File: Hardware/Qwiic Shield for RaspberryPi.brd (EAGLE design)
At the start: 52.3 x 23 mm, 22 parts, among them J1 Qwiic Right Angle, J6 Qwiic Right Angle, J7 Qwiic Right Angle, J8 Qwiic Right Angle, U2 3.3V/600mA, U3 RASPBERRY_PI

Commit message: post design review
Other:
- board text added: "v10"
- board text removed: "v01"
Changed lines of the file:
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@@
 <wire x1="51.816" y1="11.811" x2="51.308" y2="12.319" width="0.3048" layer="22"/>
 <wire x1="51.308" y1="11.303" x2="51.816" y2="11.811" width="0.3048" layer="22"/>
-<text x="48.641" y="0.508" size="1.27" layer="16" font="vector" ratio="15" rot="MR0">v01</text>
+<text x="48.641" y="0.508" size="1.27" layer="16" font="vector" ratio="15" rot="MR0">v10</text>
 <text x="21.59" y="-26.67" size="1.778" layer="51" font="vector">A. England</text>
 <dimension x1="0" y1="0" x2="0" y2="22.86" x3="-8.89" y3="11.43" textsize="1.778" layer="47" unit="inch"/>

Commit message: Updated PROD_ID of 2x20
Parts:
- U3: value RASPBERRY_PI -> (none)
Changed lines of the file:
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@@
 <element name="U$1" library="SparkFun-Aesthetics" package="SFE_LOGO_FLAME_.1" value="SFE_LOGO_FLAME.1_INCH" x="5.334" y="4.445" rot="MR0"/>
 <element name="U$2" library="SparkFun-Aesthetics" package="SFE_LOGO_NAME_.1" value="SFE_LOGO_NAME.1_INCH" x="40.767" y="4.318"/>
-<element name="U3" library="SparkFun-Connectors" package="RASPBERRY_PI_SHIELD_BOTTOM_ENTRY_NOHOLES" value="RASPBERRY_PI" x="-6.35" y="13.97"/>
+<element name="U3" library="SparkFun-Connectors" package="RASPBERRY_PI_SHIELD_BOTTOM_ENTRY_NOHOLES" value="" x="-6.35" y="13.97">
+<attribute name="PROD_ID" value="CONN-13790" x="-6.35" y="13.97" size="1.778" layer="27" display="off"/>
+<attribute name="VALUE" value="" x="-6.35" y="13.97" size="1.778" layer="27" display="off"/>
+</element>
 <element name="J12" library="SparkFun-Connectors" package="1X02_NO_SILK" value="" x="13.97" y="8.89"/>
 <element name="J2" library="SparkFun-Connectors" package="1X02_NO_SILK" value="" x="19.05" y="8.89"/>

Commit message: v20 Initial Commit
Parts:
- removed J12, J2: (no value), SparkFun-Connectors:1X02_NO_SILK
- removed J3, J5: (no value), SparkFun-Connectors:1X04_NO_SILK
- removed J4: (no value), SparkFun-Connectors:1X06_NO_SILK
- removed LOGO1: OSHW-LOGOMINI, SparkFun-Aesthetics:OSHW-LOGO-MINI
- removed U$2: SFE_LOGO_NAME.1_INCH, SparkFun-Aesthetics:SFE_LOGO_NAME_.1
- removed U3: (no value), SparkFun-Connectors:RASPBERRY_PI_SHIELD_BOTTOM_ENTRY_NOHOLES
- added H1, H2, H3, H4, H5, H6: STAND-OFFTIGHT, SparkFun-Hardware:STAND-OFF-TIGHT
- added J10: RASPBERRYPI-40-PIN-GPIO_PTH_NO_SHROUD, SparkFun-Connectors:2X20
- added LOGO3: SFE_LOGO_NAME_FLAME.2_INCH, SparkFun-Aesthetics:SFE_LOGO_NAME_FLAME_.2
- J1, J6, J7, J8: device SparkFun-Connectors:1X04_1MM_RA -> SparkFun-Connectors:JST04_1MM_RA
- U$1: value SFE_LOGO_FLAME.1_INCH -> (none); device SparkFun-Aesthetics:SFE_LOGO_FLAME_.1 -> Qwiic Hat:QWIIC_HAT0
- moved J8 32.4 mm to (59.7, 19.1), turned to 90 degrees
- moved U2 21.8 mm to (15.7, 20.8), turned to 180 degrees
- moved C1 21.0 mm to (18.6, 21.2), turned to 270 degrees
- moved J1 20.9 mm to (59.7, 10.2), turned to 90 degrees
- moved C3 17.8 mm to (17.6, 17.3), turned to 0 degrees
- moved FD1 17.7 mm to (6.52, 29.6)
- moved FD4 17.7 mm to (6.52, 29.6)
- moved J7 17.3 mm to (5.08, 10.2), turned to 270 degrees
- moved J6 15.9 mm to (5.08, 19.1), turned to 270 degrees
- moved U$1 8.05 mm to (10.0, 11.0), flipped to the top
- moved FD2 7.20 mm to (57.9, 1.34)
- moved FD3 7.20 mm to (57.9, 1.34)
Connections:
- removed net CS: J3.4, U3.24
- removed net D7: J4.1, U3.26
- new net N$1: J10.17
- new net N$2: J10.1
- net 3.3V: no longer J5.2
- net 5V: now also J10.2, J10.4; no longer J5.1, U3.2, U3.4
- net D12: now also J10.32; no longer J4.2, U3.32
- net D13: now also J10.33; no longer U3.33
- net D16: now also J10.36; no longer J4.4, U3.36
- net D17: now also J10.11; no longer U3.11
- net D18: now also J10.12; no longer U3.12
- net D19: now also J10.35; no longer U3.35
- net D20: now also J10.38; no longer J4.5, U3.38
- net D21: now also J10.40; no longer J4.6, U3.40
- net D22: now also J10.15; no longer U3.15
- net D23: now also J10.16; no longer U3.16
- net D24: now also J10.18; no longer U3.18
- net D25: now also J10.22; no longer U3.22
- net D26: now also J10.37; no longer U3.37
- net D27: now also J10.13; no longer U3.13
- net D4: now also J10.7; no longer U3.7
- net D5: now also J10.29; no longer U3.29
- net D6: now also J10.31; no longer J4.3, U3.31
- net GND: now also J10.14, J10.20, J10.25, J10.30, J10.34, J10.39, J10.6, J10.9; no longer J5.3, J5.4, U3.14, U3.20, U3.25, U3.30, U3.34, U3.39, U3.6, U3.9
- net ID_SCL: now also J10.28; no longer U3.28
- net ID_SDA: now also J10.27; no longer U3.27
- net MISO: now also J10.21; no longer J3.2, U3.21
- net MOSI: now also J10.19; no longer J3.1, U3.19
- net RX: now also J10.10; no longer J2.2, U3.10
- net SCK: now also J10.23; no longer J3.3, U3.23
- net SCL: now also J10.5; no longer J12.2, U3.5
- net SDA: now also J10.3; no longer J12.1, U3.3
- net TX: now also J10.8; no longer J2.1, U3.8
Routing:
- net SCL: track 55.7 -> 104.6 mm, vias 0 -> 4
- net 3.3V: track 46.3 -> 78.1 mm
- net SDA: track 64.1 -> 92.7 mm, vias 3 -> 4
- net RX: track 16.0 -> 0.00 mm
- net TX: track 15.6 -> 0.00 mm
- net D6: track 14.6 -> 0.00 mm
- net MISO: track 14.0 -> 0.00 mm
- net SCK: track 14.0 -> 0.00 mm
- net MOSI: track 14.0 -> 0.00 mm
- net D12: track 8.39 -> 0.00 mm
- net D16: track 8.38 -> 0.00 mm
- net D21: track 8.38 -> 0.00 mm
- net D20: track 8.38 -> 0.00 mm
- net D7: track 7.76 -> 0.00 mm
- net CS: track 7.76 -> 0.00 mm
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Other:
- board size 52.3 x 23 mm -> 65 x 30.5 mm
- board text added: "A. England and Elias Santistevan"
- board text added: "Units in MM"
- board text added: "v20"
- board text removed: "3.3V"
- board text removed: "3.3V I2C Ports"
- board text removed: "5V"
- board text removed: "A. England"
- board text removed: "CS"
- board text removed: "D12"
- board text removed: "D16"
- board text removed: "D20"
- board text removed: "D21"
- board text removed: "D6"
- board text removed: "D7"
- board text removed: "GND"
- board text removed: "MISO"
- board text removed: "MOSI"
- board text removed: "Qwiic PiHat"
- board text removed: "RX"
- board text removed: "SCK"
- board text removed: "SCL"
- board text removed: "SDA"
- board text removed: "TX"
- board text removed: "USB"
- board text removed: "v10"

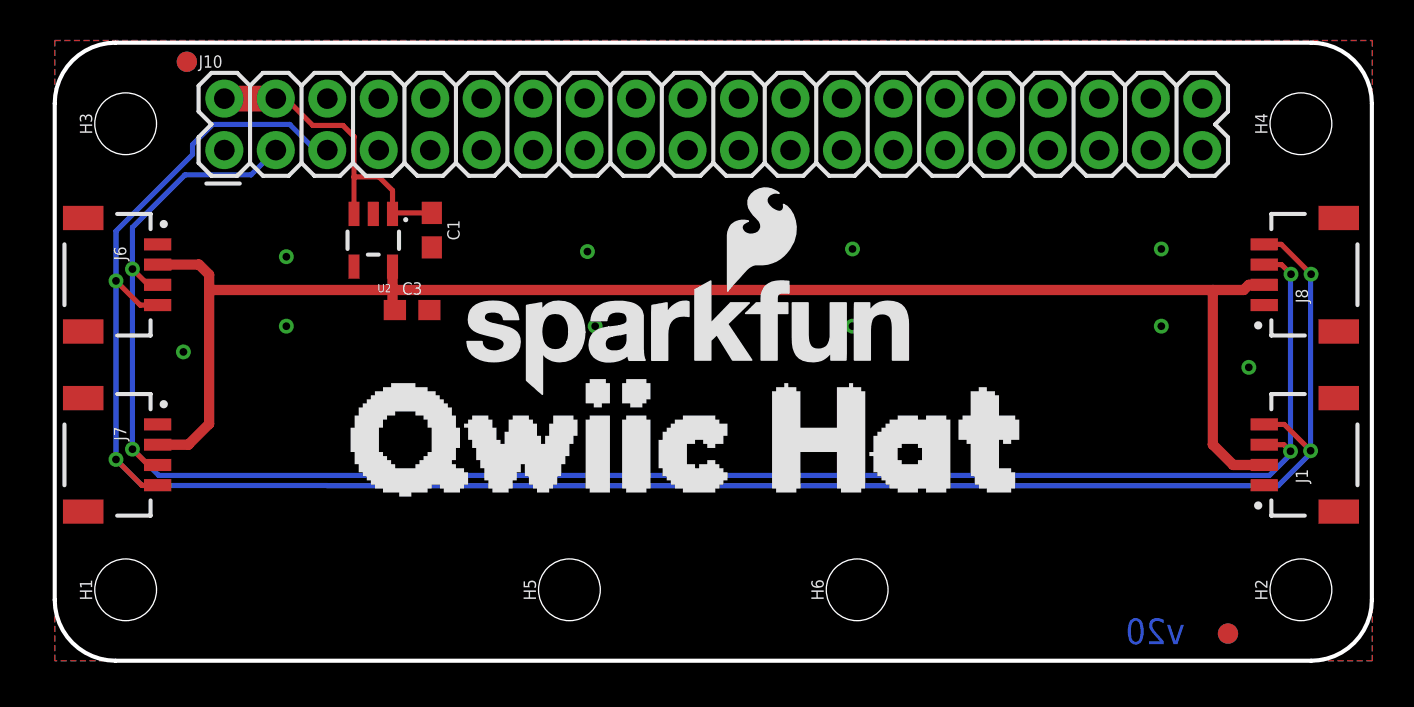
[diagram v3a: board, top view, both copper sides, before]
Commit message: Updates silk
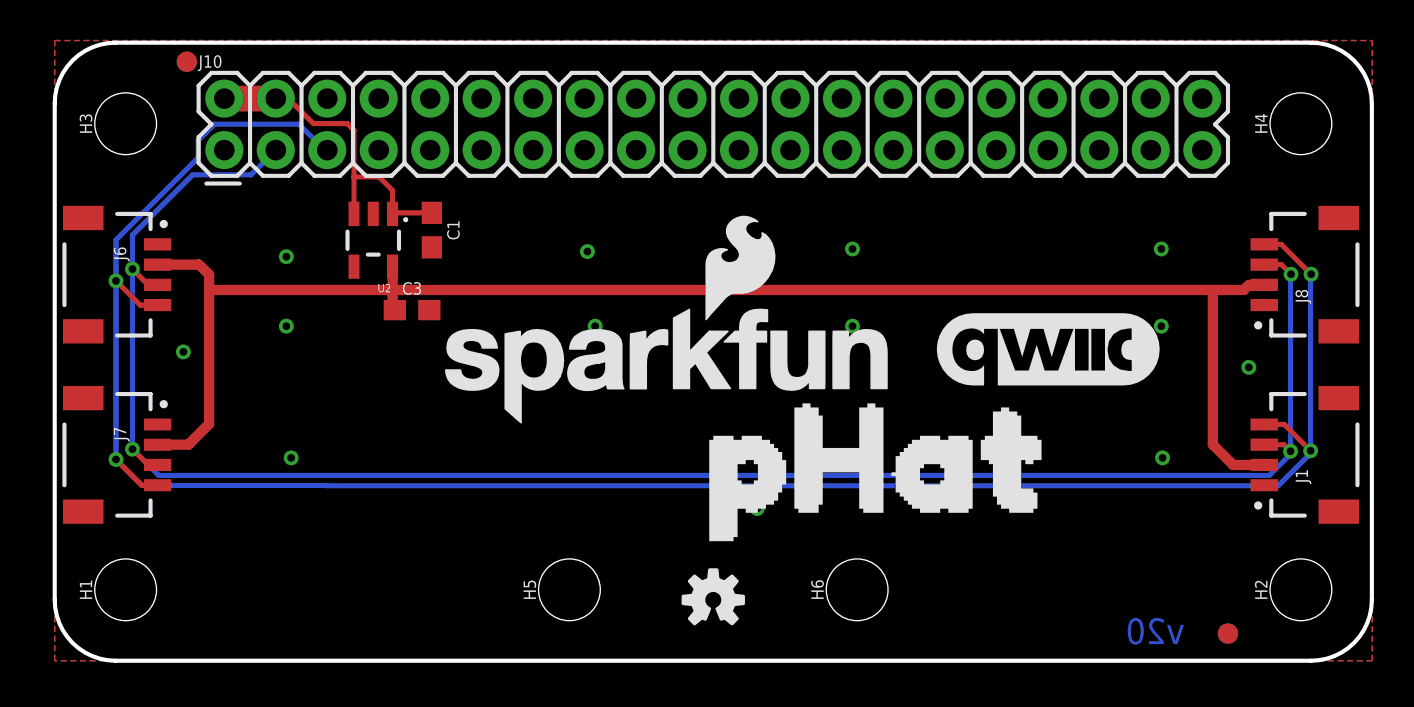
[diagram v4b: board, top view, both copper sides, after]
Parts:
- added LOGO1: SFE_LOGO_NAME_FLAME.2_INCH, SparkFun-Aesthetics:SFE_LOGO_NAME_FLAME_.2
- added U$3: (no value), MicroPiHat:PHAT0
- LOGO3: value SFE_LOGO_NAME_FLAME.2_INCH -> OSHW-LOGOS; device SparkFun-Aesthetics:SFE_LOGO_NAME_FLAME_.2 -> SparkFun-Aesthetics:OSHW-LOGO-S
- U$1: device Qwiic Hat:QWIIC_HAT0 -> SparkFun-Aesthetics:QWIIC_11MM
- moved U$1 39.3 mm to (49.1, 15.3)
- moved LOGO3 13.0 mm to (32.5, 3.00)
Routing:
- net 3.3V: track 78.1 -> 77.3 mm
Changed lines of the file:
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@@
 <setting verticaltext="up"/>
 </settings>
-<grid distance="1" unitdist="mm" unit="mm" style="lines" multiple="1" display="yes" altdistance="0.1" altunitdist="mm" altunit="mm"/>
+<grid distance="0.5" unitdist="mm" unit="mm" style="lines" multiple="1" display="yes" altdistance="0.01" altunitdist="mm" altunit="mm"/>
 <layers>
 <layer number="1" name="Top" color="4" fill="1" visible="yes" active="yes"/>
@@
 <layer number="14" name="Route14" color="1" fill="6" visible="no" active="no"/>
 <layer number="15" name="Route15" color="4" fill="6" visible="no" active="no"/>
-<layer number="16" name="Bottom" color="1" fill="1" visible="yes" active="yes"/>
-<layer number="17" name="Pads" color="2" fill="1" visible="yes" active="yes"/>
+<layer number="16" name="Bottom" color="31" fill="1" visible="yes" active="yes"/>
+<layer number="17" name="Pads" color="30" fill="1" visible="yes" active="yes"/>
 <layer number="18" name="Vias" color="2" fill="1" visible="yes" active="yes"/>
 <layer number="19" name="Unrouted" color="6" fill="1" visible="yes" active="yes"/>
@@
 <layer number="45" name="Holes" color="7" fill="1" visible="yes" active="yes"/>
 <layer number="46" name="Milling" color="3" fill="1" visible="no" active="yes"/>
-<layer number="47" name="Measures" color="7" fill="1" visible="yes" active="yes"/>
+<layer number="47" name="Measures" color="7" fill="1" visible="no" active="yes"/>
 <layer number="48" name="Document" color="7" fill="1" visible="no" active="yes"/>
-<layer number="49" name="Reference" color="26" fill="1" visible="yes" active="yes"/>
+<layer number="49" name="Reference" color="13" fill="1" visible="yes" active="yes"/>
 <layer number="50" name="dxf" color="7" fill="1" visible="no" active="yes"/>
 <layer number="51" name="tDocu" color="6" fill="1" visible="yes" active="yes"/>
@@
 <layer number="115" name="ReferenceISLANDS" color="7" fill="1" visible="no" active="yes"/>
 <layer number="116" name="Patch_BOT" color="9" fill="4" visible="no" active="yes"/>
+<layer number="117" name="PM_Ref" color="26" fill="1" visible="no" active="yes"/>
 <layer number="118" name="Rect_Pads" color="7" fill="1" visible="no" active="yes"/>
+<layer number="119" name="PF_Ref" color="31" fill="1" visible="no" active="yes"/>
+<layer number="120" name="WFL_Ref" color="25" fill="1" visible="no" active="yes"/>
 <layer number="121" name="_tsilk" color="7" fill="1" visible="no" active="yes"/>
 <layer number="122" name="_bsilk" color="7" fill="1" visible="no" active="yes"/>
@@
 <circle x="25.4" y="3.5" radius="3.15" width="0" layer="41"/>
 <text x="21" y="-11" size="2" layer="47" font="vector">Units in MM</text>
+<dimension x1="3.5" y1="3.5" x2="3.5" y2="26.5" x3="-2" y3="15" textsize="1.778" textratio="15" layer="47"/>
 </plain>
 <attributes>
@@
 <attribute name="VALUE" x="41.251" y="3.5" size="0.6096" layer="27" font="vector" ratio="20" rot="R90" align="top-center"/>
 </element>
-<element name="LOGO3" library="SparkFun-Aesthetics" package="SFE_LOGO_NAME_FLAME_.2" value="SFE_LOGO_NAME_FLAME.2_INCH" x="31.32" y="15.97" smashed="yes"/>
-<element name="U$1" library="Qwiic Hat" package="QWIIC_HAT0" value="" x="10" y="11" smashed="yes"/>
+<element name="U$1" library="SparkFun-Aesthetics" package="QWIIC_11MM" value="" x="49.054" y="15.32" smashed="yes"/>
+<element name="LOGO1" library="SparkFun-Aesthetics" package="SFE_LOGO_NAME_FLAME_.2" value="SFE_LOGO_NAME_FLAME.2_INCH" x="30.266" y="14.566" smashed="yes"/>
+<element name="LOGO3" library="SparkFun-Aesthetics" package="OSHW-LOGO-S" value="OSHW-LOGOS" x="32.5" y="3" smashed="yes"/>
+<element name="U$3" library="MicroPiHat" package="PHAT0" value="" x="27.5" y="10" smashed="yes"/>
 </elements>
 <signals>
@@
 <via x="39.37" y="16.51" extent="1-16" drill="0.381"/>
 <via x="39.37" y="20.32" extent="1-16" drill="0.381"/>
+<via x="11.67" y="10.01" extent="1-16" drill="0.381"/>
+<via x="34.67" y="7.51" extent="1-16" drill="0.381"/>
+<via x="54.67" y="10.01" extent="1-16" drill="0.381"/>
 </signal>
 <signal name="3.3V">
@@
 <wire x1="16.67" y1="18.296" x2="16.67" y2="18.288" width="0.508" layer="1"/>
 <wire x1="16.67" y1="18.288" x2="16.67" y2="17.422" width="0.508" layer="1"/>
-<wire x1="59.69" y1="18.55" x2="58.928" y2="18.55" width="0.508" layer="1"/>
 <wire x1="58.928" y1="18.55" x2="58.674" y2="18.296" width="0.508" layer="1"/>
 <wire x1="58.674" y1="18.296" x2="57.15" y2="18.296" width="0.508" layer="1"/>
@@
 <wire x1="7.62" y1="18.296" x2="7.62" y2="11.684" width="0.508" layer="1"/>
 <wire x1="16.67" y1="18.296" x2="7.62" y2="18.296" width="0.508" layer="1"/>
+<wire x1="58.928" y1="18.55" x2="59.69" y2="18.55" width="0" layer="19" extent="1-1"/>
 </signal>
 <signal name="SDA">
@@
 <wire x1="59.944" y1="9.144" x2="60.9854" y2="10.1854" width="0.254" layer="16"/>
 <wire x1="10.91" y1="25.2" x2="9.6876" y2="23.9776" width="0.254" layer="16"/>
-<wire x1="9.6876" y1="23.9776" x2="6.4262" y2="23.9776" width="0.254" layer="16"/>
-<wire x1="6.4262" y1="23.9776" x2="3.8354" y2="21.3868" width="0.254" layer="16"/>
-<wire x1="3.8354" y1="21.3868" x2="3.8354" y2="19.3294" width="0.254" layer="16"/>
+<wire x1="9.6876" y1="23.9776" x2="6.8072" y2="23.9776" width="0.254" layer="16"/>
+<wire x1="6.8072" y1="23.9776" x2="3.8354" y2="21.0058" width="0.254" layer="16"/>
+<wire x1="3.8354" y1="21.0058" x2="3.8354" y2="19.3294" width="0.254" layer="16"/>
 <wire x1="3.8354" y1="10.4394" x2="5.1308" y2="9.144" width="0.254" layer="16"/>
 <wire x1="5.1308" y1="9.144" x2="59.944" y2="9.144" width="0.254" layer="16"/>
@@
 <wire x1="61.976" y1="10.2362" x2="60.3758" y2="8.636" width="0.254" layer="16"/>
 <wire x1="13.45" y1="8.648" x2="13.462" y2="8.636" width="0.254" layer="16"/>
-<wire x1="3.0226" y1="18.7452" x2="3.0226" y2="21.2" width="0.254" layer="16"/>
-<wire x1="11.599" y1="26.4668" x2="7.7978" y2="26.4668" width="0.254" layer="16"/>
-<wire x1="13.45" y1="25.2" x2="12.8658" y2="25.2" width="0.254" layer="16"/>
-<wire x1="12.8658" y1="25.2" x2="11.599" y2="26.4668" width="0.254" layer="16"/>
+<wire x1="3.0226" y1="18.7452" x2="3.0226" y2="20.7682" width="0.254" layer="16"/>
+<wire x1="12.049" y1="26.4768" x2="7.884" y2="26.4768" width="0.254" layer="16"/>
+<wire x1="13.45" y1="25.2" x2="13.3258" y2="25.2" width="0.254" layer="16"/>
+<wire x1="13.3258" y1="25.2" x2="12.049" y2="26.4768" width="0.254" layer="16"/>
 <wire x1="5.08" y1="17.55" x2="4.2178" y2="17.55" width="0.254" layer="1"/>
 <wire x1="4.2178" y1="17.55" x2="3.0226" y2="18.7452" width="0.254" layer="1"/>
 <wire x1="3.0226" y1="9.9314" x2="4.294" y2="8.66" width="0.254" layer="1"/>
 <wire x1="4.294" y1="8.66" x2="5.08" y2="8.66" width="0.254" layer="1"/>
-<wire x1="6.8" y1="25.469" x2="7.7978" y2="26.4668" width="0.254" layer="16"/>
-<wire x1="3.0226" y1="21.2" x2="6.8" y2="24.9774" width="0.254" layer="16"/>
-<wire x1="6.8" y1="24.9774" x2="6.8" y2="25.469" width="0.254" layer="16"/>
+<wire x1="7.0794" y1="25.6722" x2="7.884" y2="26.4768" width="0.254" layer="16"/>
+<wire x1="3.0226" y1="20.7682" x2="7.0794" y2="24.825" width="0.254" layer="16"/>
+<wire x1="7.0794" y1="24.825" x2="7.0794" y2="25.6722" width="0.254" layer="16"/>
 </signal>
 <signal name="5V">
@@
 <wire x1="16.7199" y1="22.1" x2="16.67" y2="22.0501" width="0.254" layer="1"/>
 <wire x1="14.77" y1="22.0501" x2="14.769996875" y2="22.050103125" width="0.254" layer="1"/>
-<wire x1="12.734" y1="26.416" x2="11.41" y2="27.74" width="0.254" layer="1"/>
-<wire x1="10.91" y1="27.74" x2="11.41" y2="27.74" width="0.254" layer="1"/>
-<wire x1="12.734" y1="26.416" x2="14.224" y2="26.416" width="0.254" layer="1"/>
-<wire x1="14.224" y1="26.416" x2="14.77" y2="25.87" width="0.254" layer="1"/>
-<wire x1="14.77" y1="25.87" x2="14.77" y2="23.876" width="0.254" layer="1"/>
+<wire x1="12.764" y1="26.506" x2="11.53" y2="27.74" width="0.254" layer="1"/>
+<wire x1="11.53" y1="27.74" x2="10.91" y2="27.74" width="0.254" layer="1"/>
+<wire x1="12.764" y1="26.506" x2="14.434" y2="26.506" width="0.254" layer="1"/>
+<wire x1="14.434" y1="26.506" x2="14.77" y2="26.17" width="0.254" layer="1"/>
+<wire x1="14.77" y1="26.17" x2="14.77" y2="23.876" width="0.254" layer="1"/>
 <wire x1="14.77" y1="23.876" x2="14.77" y2="22.0501" width="0.254" layer="1"/>
 <wire x1="16.67" y1="22.0501" x2="16.67" y2="23.208" width="0.254" layer="1"/>

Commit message: Adjusts 1 inch spaced drill hits, adds seperation line to schematic
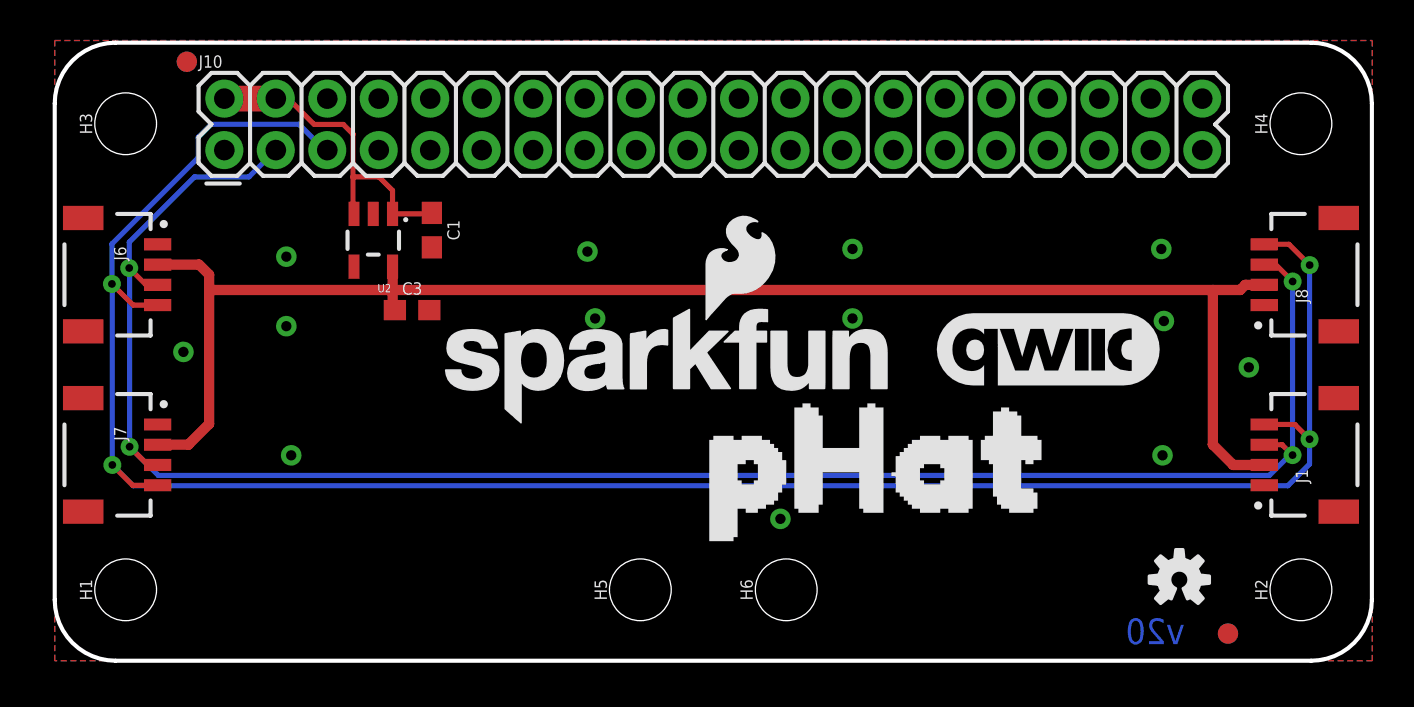
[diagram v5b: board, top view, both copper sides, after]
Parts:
- moved LOGO3 23.0 mm to (55.5, 4.00)
- moved H5 3.50 mm to (28.9, 3.50)
- moved H6 3.50 mm to (36.1, 3.50)
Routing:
- net SCL: track 104.6 -> 105.4 mm
- net 3.3V: track 77.3 -> 78.0 mm
- net SDA: track 92.5 -> 93.0 mm
